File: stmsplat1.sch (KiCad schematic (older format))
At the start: 72 parts, among them CN1 Conn_01x16_Male, CN2 Conn_01x30_Male, CN3 Conn_01x20_Male, CN4 Conn_01x34_Male, J1 Conn_Coaxial, J2 Conn_01x04_Male, J3 Conn_01x04_Male, U1 NUCLEO144-F746ZG, U10 MPL315A2, U11 XBee3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

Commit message: 2nd go at manual routing. Via sizes may all be small.
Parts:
- added C21: 100uF, Capacitor_THT:CP_Radial_D5.0mm_P2.50mm, symbol Device:CP
- U11: symbol splatlib:XBee3 -> stmsplat1-rescue:XBee3-splatlib
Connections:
- net 5V0 is gone; now on net +5V: J2.1 (Pin_1), J3.1 (Pin_1)
- net +5V: now also C21.1
- net GND: now also C21.2
- net at D8.2 (A): now also U11.5 (~RESET)
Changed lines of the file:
@@
 	7550 10450 7900 10450
 Text HLabel 7900 10150 2    50   Input ~ 0
-5V0
++5V
 Text HLabel 7900 10250 2    50   Input ~ 0
 PC12
@@
 	8350 8100 8350 8000
 $Comp
-L splatlib:XBee3 U11
+L stmsplat1-rescue:XBee3-splatlib U11
 U 1 1 5BFA172B
 P 7350 7600
@@
 Connection ~ 12250 8950
 Wire Wire Line
-	10700 8250 10300 8250
+	10700 8250 10500 8250
 $Comp
 L Device:C C20
@@
 	7550 9600 7900 9600
 Text HLabel 7900 9300 2    50   Input ~ 0
-5V0
++5V
 Text HLabel 7900 9400 2    50   Input ~ 0
 PD6
@@
 Wire Wire Line
 	8500 6400 8500 6200
+$Comp
+L Device:CP C21
+U 1 1 5C1EE7CD
+P 10500 8700
+F 0 "C21" H 10618 8746 50  0000 L CNN
+F 1 "100uF" H 10618 8655 50  0000 L CNN
+F 2 "Capacitor_THT:CP_Radial_D5.0mm_P2.50mm" H 10538 8550 50  0001 C CNN
+F 3 "~" H 10500 8700 50  0001 C CNN
+	1    10500 8700
+	1    0    0    -1
+$EndComp
+Wire Wire Line
+	10500 8850 10500 8950
+Wire Wire Line
+	11000 8950 10500 8950
+Connection ~ 11000 8950
+Wire Wire Line
+	10500 8550 10500 8250
+Connection ~ 10500 8250
+Wire Wire Line
+	10500 8250 10300 8250
 $EndSCHEMATC

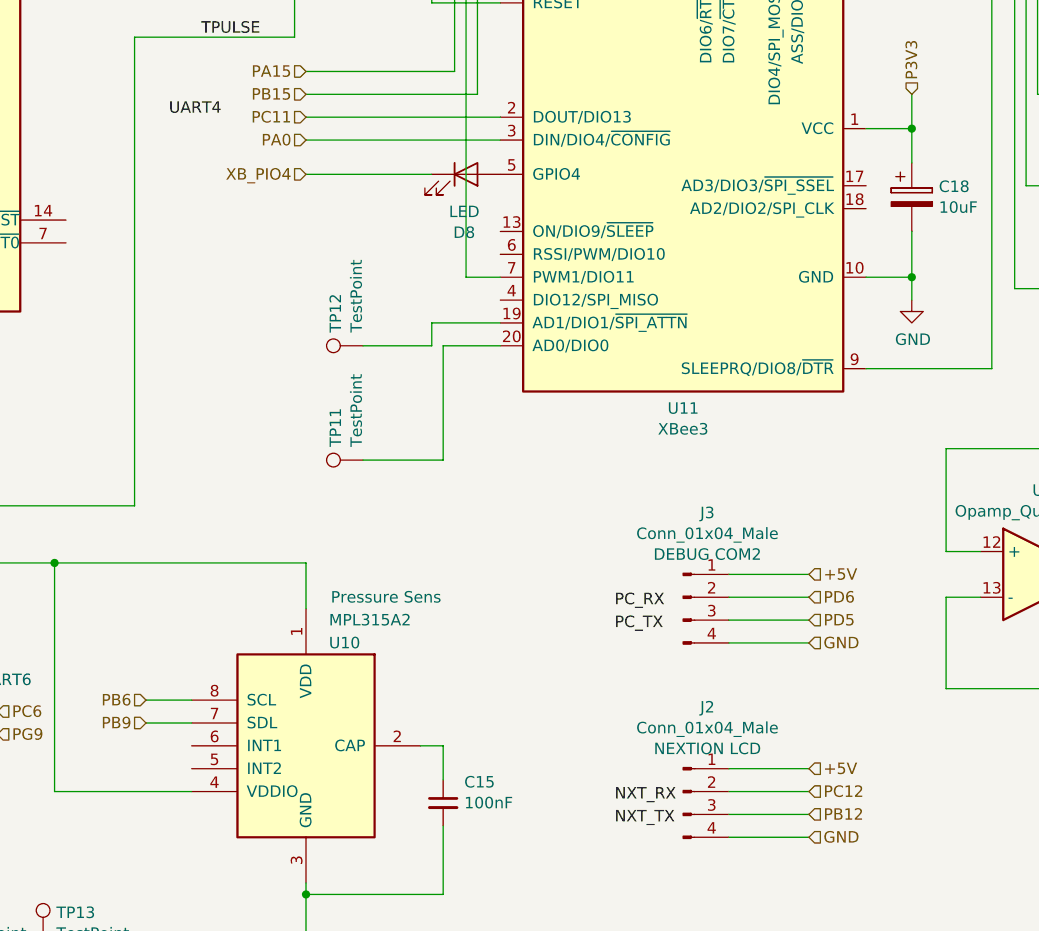
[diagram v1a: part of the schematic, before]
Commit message: Fix Xbee extra symbol pin, change via sizes on power
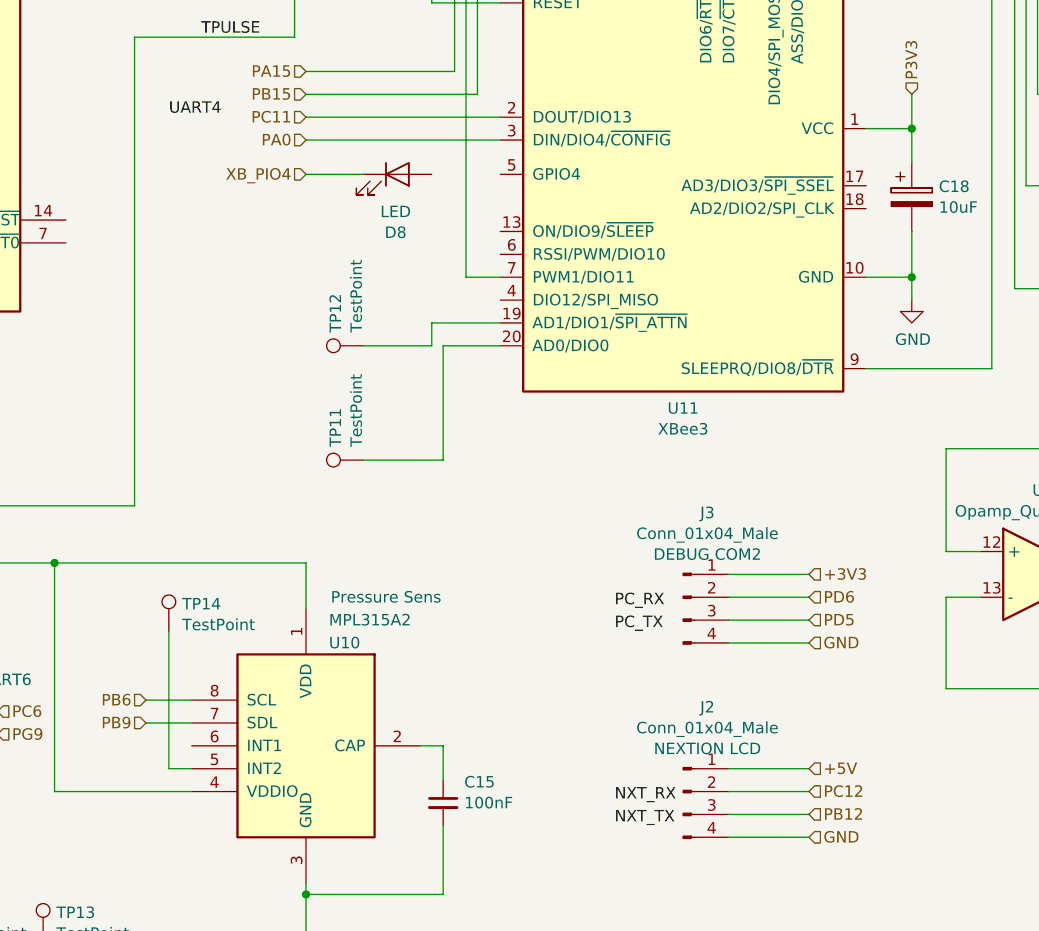
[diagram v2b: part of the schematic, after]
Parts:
- added TP14: TestPoint, TestPoint:TestPoint_Loop_D1.80mm_Drill1.0mm_Beaded, symbol Connector:TestPoint
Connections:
- net +3V3: now also J3.1 (Pin_1)
- net +5V: no longer J3.1 (Pin_1)
- net at U10.5 (INT2): now also TP14.1
- net at D8.2 (A): no longer U11.5 (~RESET)
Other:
- moved on the sheet: D8
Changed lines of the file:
@@
 L Device:LED D8
 U 1 1 5C2D017B
-P 6400 7550
-F 0 "D8" H 6392 7295 50  0000 C CNN
-F 1 "LED" H 6392 7386 50  0000 C CNN
-F 2 "LED_SMD:LED_PLCC-2" H 6400 7550 50  0001 C CNN
-F 3 "~" H 6400 7550 50  0001 C CNN
-	1    6400 7550
-	1    0    0    -1
-$EndComp
-Wire Wire Line
-	6250 7550 5700 7550
+P 6100 7550
+F 0 "D8" H 6092 7295 50  0000 C CNN
+F 1 "LED" H 6092 7386 50  0000 C CNN
+F 2 "LED_SMD:LED_PLCC-2" H 6100 7550 50  0001 C CNN
+F 3 "~" H 6100 7550 50  0001 C CNN
+	1    6100 7550
+	1    0    0    -1
+$EndComp
+Wire Wire Line
+	5950 7550 5700 7550
 Text HLabel 13250 1400 0    50   Input ~ 0
 XB_PIO4
@@
 	7550 9600 7900 9600
 Text HLabel 7900 9300 2    50   Input ~ 0
-+5V
++3V3
 Text HLabel 7900 9400 2    50   Input ~ 0
 PD6
@@
 Wire Wire Line
 	10500 8250 10300 8250
+$Comp
+L Connector:TestPoint TP14
+U 1 1 5C244655
+P 5100 9550
+F 0 "TP14" H 5158 9670 50  0000 L CNN
+F 1 "TestPoint" H 5158 9579 50  0000 L CNN
+F 2 "TestPoint:TestPoint_Loop_D1.80mm_Drill1.0mm_Beaded" H 5300 9550 50  0001 C CNN
+F 3 "~" H 5300 9550 50  0001 C CNN
+	1    5100 9550
+	1    0    0    -1
+$EndComp
+Wire Wire Line
+	5200 10150 5100 10150
+Wire Wire Line
+	5100 10150 5100 9550
 $EndSCHEMATC

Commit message: Update schematic
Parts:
- removed U11: XBee3, spatboard:XBEE-22MM-TH, symbol stmsplat1-rescue:XBee3-splatlib
- added U11: XBee3, spatboard:XBEE-22MM-TH, symbol splatlib:XBee3
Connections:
- net GND: now also U11.10 (GND)
- net P3V3: now also U11.1 (VCC)
- net PA0: now also U11.3 (DIN/DIO4/~CONFIG)
- net PA15: now also U11.12 (DIO7/~CTS)
- net PB15: now also U11.16 (DIO6/~RTS)
- net PC11: now also U11.2 (DOUT/DIO13)
- net PE10: now also U11.9 (SLEEPRQ/DIO8/~DTR)
- net PE15: now also U11.5 (~RESET)
- net at TP12.1: now also U11.19 (AD1/DIO1/~SPI_ATTN)
- net at TP11.1: now also U11.20 (AD0/DIO0)
- net at U8.9: now also U11.7 (PWM1/DIO11)
- net at D8.2 (A): now also U11.13 (ON/DIO9/~SLEEP)
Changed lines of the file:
@@
 Wire Wire Line
 	8350 8100 8350 8000
-$Comp
-L stmsplat1-rescue:XBee3-splatlib U11
-U 1 1 5BFA172B
-P 7350 7600
-F 0 "U11" H 7350 6626 50  0000 C CNN
-F 1 "XBee3" H 7350 6535 50  0000 C CNN
-F 2 "spatboard:XBEE-22MM-TH" H 7500 7700 50  0001 C CNN
-F 3 "http://www.ti.com/lit/gpn/cc2520" H 7350 7350 50  0001 C CNN
-	1    7350 7600
-	1    0    0    -1
-$EndComp
 Wire Wire Line
 	7550 6600 7550 6400
@@
 Wire Wire Line
 	5100 10150 5100 9550
+$Comp
+L splatlib:XBee3 U11
+U 1 1 5C4E2737
+P 7350 7600
+F 0 "U11" H 7350 6626 50  0000 C CNN
+F 1 "XBee3" H 7350 6535 50  0000 C CNN
+F 2 "spatboard:XBEE-22MM-TH" H 7500 7700 50  0001 C CNN
+F 3 "http://www.ti.com/lit/gpn/cc2520" H 7350 7350 50  0001 C CNN
+	1    7350 7600
+	1    0    0    -1
+$EndComp
+Wire Wire Line
+	6550 7800 6350 7800
+Wire Wire Line
+	6350 7800 6350 7550
+Wire Wire Line
+	6350 7550 6250 7550
 $EndSCHEMATC

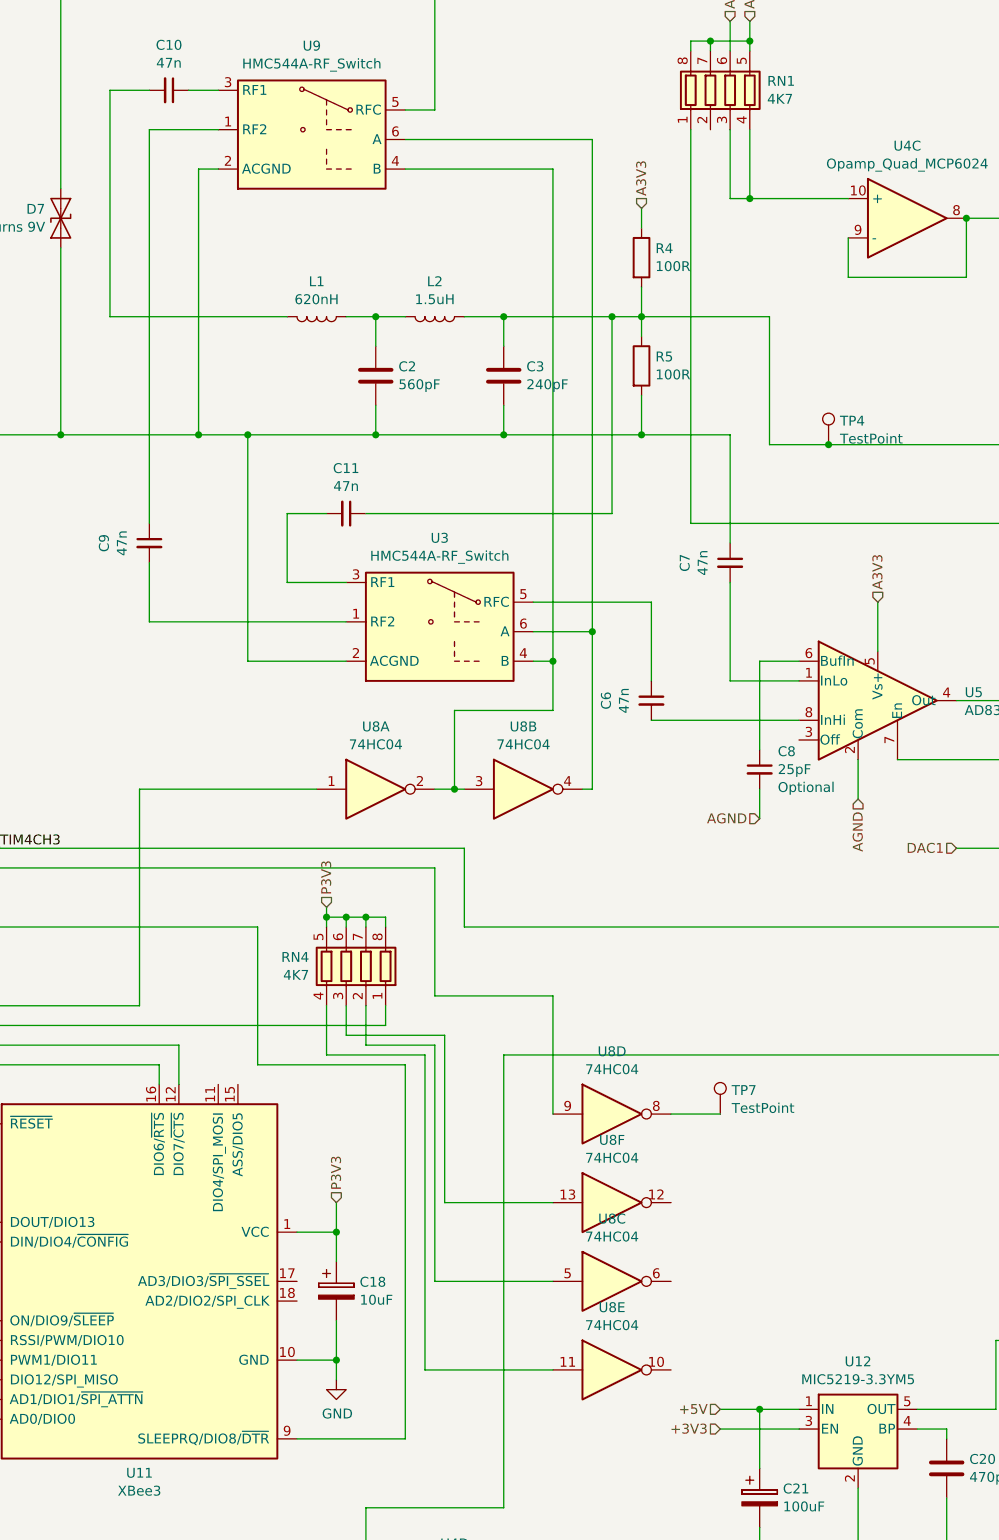
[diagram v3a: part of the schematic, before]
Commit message: Split drive to RF switches
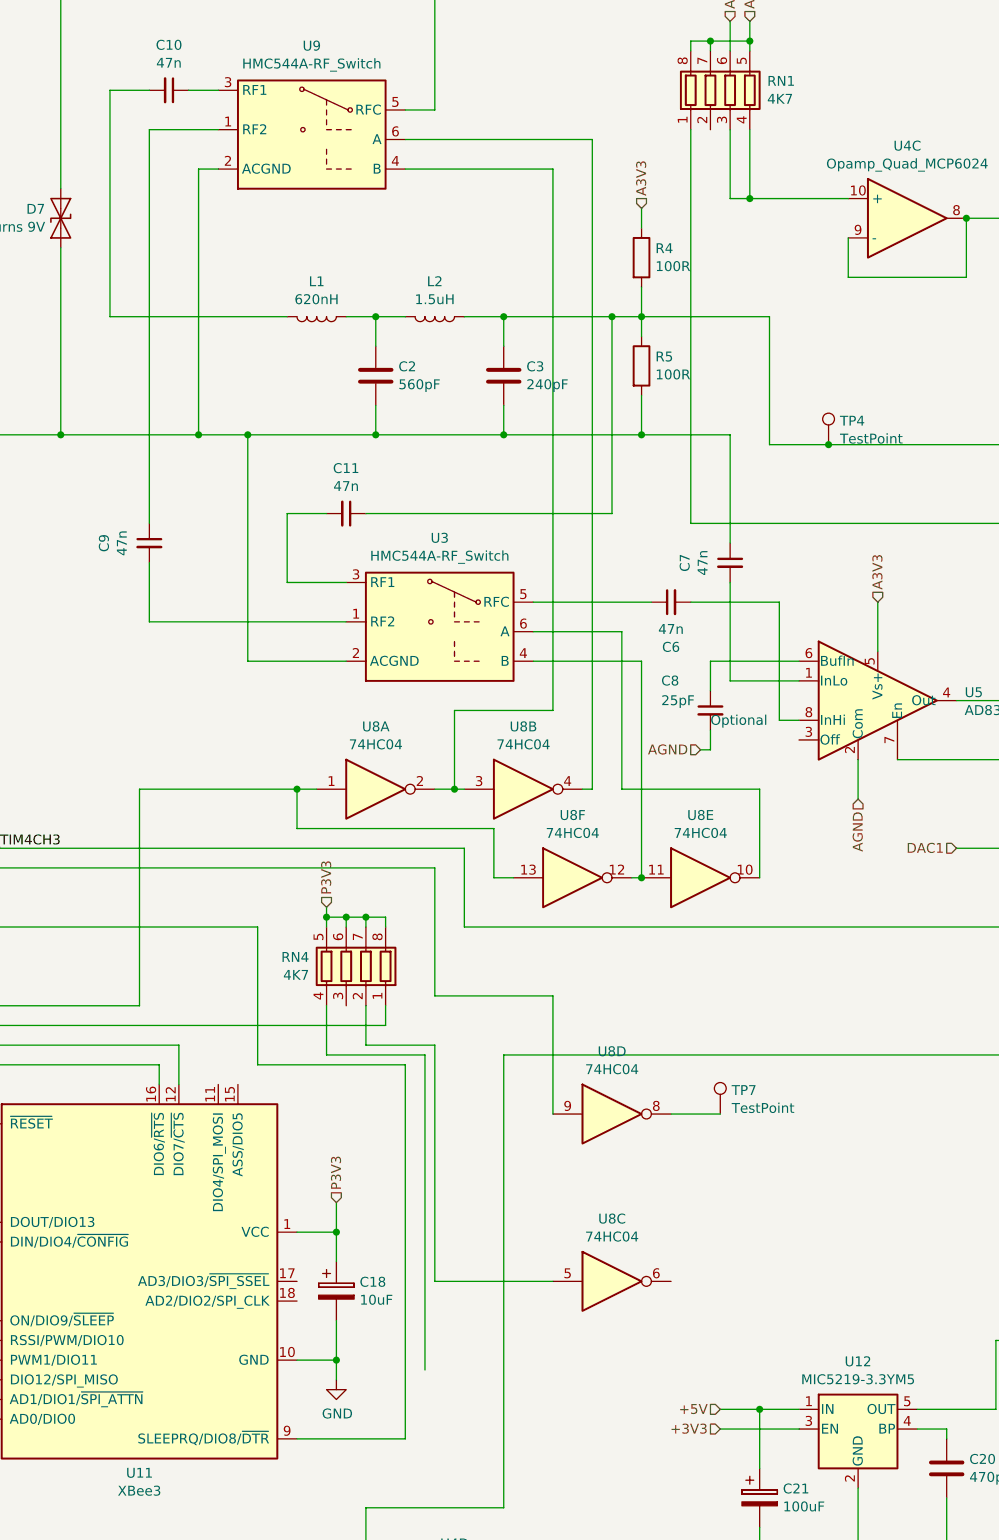
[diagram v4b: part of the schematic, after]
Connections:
- net PE14: now also U8.13
- net at U8.2, U8.3, U9.4 (B): no longer U3.4 (B)
- net at U8.4, U9.6 (A): no longer U3.6 (A)
- net at U8.10: now also U3.6 (A)
- net at U8.11: now also U3.4 (B), U8.12; no longer RN4.4 (R4.1)
- net at RN4.3 (R3.1): no longer U8.13
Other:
- moved on the sheet: C6, C8, U8E, U8F
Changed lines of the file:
@@
 L Device:C_Small C6
 U 1 1 5BFDF984
-P 9950 4650
-F 0 "C6" V 9721 4650 50  0000 C CNN
-F 1 "47n" V 9812 4650 50  0000 C CNN
-F 2 "Capacitor_SMD:C_1210_3225Metric_Pad1.42x2.65mm_HandSolder" H 9950 4650 50  0001 C CNN
-F 3 "~" H 9950 4650 50  0001 C CNN
-	1    9950 4650
-	1    0    0    -1
+P 10050 4150
+F 0 "C6" V 9821 4150 50  0000 C CNN
+F 1 "47n" V 9912 4150 50  0000 C CNN
+F 2 "Capacitor_SMD:C_1210_3225Metric_Pad1.42x2.65mm_HandSolder" H 10050 4150 50  0001 C CNN
+F 3 "~" H 10050 4150 50  0001 C CNN
+	1    10050 4150
+	0    -1   -1   0
 $EndComp
 Wire Wire Line
@@
 	6950 2350 6950 3300
 Connection ~ 6950 3300
-$Comp
-L Device:C_Small C8
-U 1 1 5BEE1C9A
-P 10500 5000
-F 0 "C8" H 10592 5091 50  0000 L CNN
-F 1 "25pF" H 10592 5000 50  0000 L CNN
-F 2 "Capacitor_THT:C_Disc_D7.5mm_W2.5mm_P5.00mm" H 10500 5000 50  0001 C CNN
-F 3 "~" H 10500 5000 50  0001 C CNN
-F 4 "Optional" H 10592 4909 50  0000 L CNN "Option"
-	1    10500 5000
-	1    0    0    -1
-$EndComp
-Wire Wire Line
-	10500 5100 10500 5250
-Text HLabel 10500 5250 0    50   Input ~ 0
+Text HLabel 10200 4900 0    50   Input ~ 0
 AGND
-Wire Wire Line
-	10700 4450 10500 4450
-Wire Wire Line
-	10500 4450 10500 4900
 $Comp
 L 74xx:74HC04 U8
@@
 Connection ~ 11550 2200
 Wire Wire Line
-	9950 4150 9950 4550
-Wire Wire Line
 	7750 1950 7650 1950
 Wire Wire Line
@@
 L 74xx:74HC04 U8
 U 5 1 5C133549
-P 9750 8050
-F 0 "U8" H 9750 8367 50  0000 C CNN
-F 1 "74HC04" H 9750 8276 50  0000 C CNN
-F 2 "" H 9750 8050 50  0001 C CNN
-F 3 "http://www.nxp.com/documents/data_sheet/74HC_HCT04.pdf" H 9750 8050 50  0001 C CNN
-	5    9750 8050
+P 10200 5550
+F 0 "U8" H 10200 5867 50  0000 C CNN
+F 1 "74HC04" H 10200 5776 50  0000 C CNN
+F 2 "" H 10200 5550 50  0001 C CNN
+F 3 "http://www.nxp.com/documents/data_sheet/74HC_HCT04.pdf" H 10200 5550 50  0001 C CNN
+	5    10200 5550
 	1    0    0    -1
 $EndComp
@@
 L 74xx:74HC04 U8
 U 6 1 5C133550
-P 9750 7200
-F 0 "U8" H 9750 7517 50  0000 C CNN
-F 1 "74HC04" H 9750 7426 50  0000 C CNN
-F 2 "" H 9750 7200 50  0001 C CNN
-F 3 "http://www.nxp.com/documents/data_sheet/74HC_HCT04.pdf" H 9750 7200 50  0001 C CNN
-	6    9750 7200
+P 9550 5550
+F 0 "U8" H 9550 5867 50  0000 C CNN
+F 1 "74HC04" H 9550 5776 50  0000 C CNN
+F 2 "" H 9550 5550 50  0001 C CNN
+F 3 "http://www.nxp.com/documents/data_sheet/74HC_HCT04.pdf" H 9550 5550 50  0001 C CNN
+	6    9550 5550
 	1    0    0    -1
 $EndComp
 Wire Wire Line
 	9600 5100 9650 5100
-Wire Wire Line
-	9650 5100 9650 4300
-Wire Wire Line
-	9650 4300 9350 4300
-Wire Wire Line
-	9350 4450 9450 4450
-Wire Wire Line
-	9450 4450 9450 4700
 Wire Wire Line
 	9450 4700 8950 4700
@@
 	8200 950  8850 950
 Wire Wire Line
-	9650 4300 9650 1800
-Wire Wire Line
 	9650 1800 8700 1800
-Connection ~ 9650 4300
-Wire Wire Line
-	9450 4450 9450 1950
 Wire Wire Line
 	8700 1950 9450 1950
-Connection ~ 9450 4450
 Connection ~ 10850 3350
 Wire Wire Line
@@
 NXT_RX
 Wire Wire Line
-	8250 5100 7350 5100
+	8250 5100 8150 5100
 Wire Wire Line
 	7350 5100 7350 6200
@@
 	13550 8950 13900 8950
 Wire Wire Line
-	9450 8050 8800 8050
-Wire Wire Line
 	8800 8050 8800 6450
 Wire Wire Line
@@
 Wire Wire Line
 	8850 6400 8500 6400
-Wire Wire Line
-	9450 7200 8900 7200
-Wire Wire Line
-	8900 7200 8900 6350
 Wire Wire Line
 	8400 5750 8500 5750
@@
 Wire Wire Line
 	10350 4050 10350 4550
-Wire Wire Line
-	9950 4750 10700 4750
 Wire Wire Line
 	6150 950  6400 950
@@
 	5650 6300 8600 6300
 Wire Wire Line
-	8400 6350 8400 6200
-Wire Wire Line
-	8400 6350 8900 6350
-Wire Wire Line
 	8500 6400 8500 6200
 $Comp
@@
 Wire Wire Line
 	6350 7550 6250 7550
+Wire Wire Line
+	9450 1950 9450 4700
+Wire Wire Line
+	9350 4450 9900 4450
+Wire Wire Line
+	9900 4450 9900 5550
+Wire Wire Line
+	9900 5550 9850 5550
+Wire Wire Line
+	8150 5100 8150 5300
+Wire Wire Line
+	8150 5300 9150 5300
+Wire Wire Line
+	9150 5300 9150 5550
+Wire Wire Line
+	9150 5550 9250 5550
+Connection ~ 8150 5100
+Wire Wire Line
+	8150 5100 7350 5100
+Wire Wire Line
+	9650 1800 9650 5100
+Connection ~ 9900 5550
+$Comp
+L Device:C_Small C8
+U 1 1 5BEE1C9A
+P 10250 4700
+F 0 "C8" H 10000 4850 50  0000 L CNN
+F 1 "25pF" H 10000 4750 50  0000 L CNN
+F 2 "Capacitor_THT:C_Disc_D7.5mm_W2.5mm_P5.00mm" H 10250 4700 50  0001 C CNN
+F 3 "~" H 10250 4700 50  0001 C CNN
+F 4 "Optional" H 10250 4650 50  0000 L CNN "Option"
+	1    10250 4700
+	1    0    0    -1
+$EndComp
+Wire Wire Line
+	10700 4450 10250 4450
+Wire Wire Line
+	10250 4900 10200 4900
+Wire Wire Line
+	10150 4150 10600 4150
+Wire Wire Line
+	10600 4150 10600 4750
+Wire Wire Line
+	10600 4750 10700 4750
+Wire Wire Line
+	9800 5100 9800 4300
+Wire Wire Line
+	9800 4300 9350 4300
+Wire Wire Line
+	10500 5550 10500 5100
+Wire Wire Line
+	9800 5100 10500 5100
+Wire Wire Line
+	10250 4450 10250 4600
+Wire Wire Line
+	10250 4800 10250 4900
 $EndSCHEMATC

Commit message: Prepared for PCB production
Several PCB tracking changes and footprint tweaks etc
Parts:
- J2, J3: footprint Connector_PinHeader_2.54mm:PinHeader_1x04_P2.54mm_Vertical -> spatboard:PinHeader_1x04_P2.54mm_Vertical
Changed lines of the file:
@@
 F 0 "J2" H 7456 10619 50  0000 C CNN
 F 1 "Conn_01x04_Male" H 7456 10528 50  0000 C CNN
-F 2 "Connector_PinHeader_2.54mm:PinHeader_1x04_P2.54mm_Vertical" H 7350 10250 50  0001 C CNN
+F 2 "spatboard:PinHeader_1x04_P2.54mm_Vertical" H 7350 10250 50  0001 C CNN
 F 3 "~" H 7350 10250 50  0001 C CNN
 F 4 "NEXTION LCD" H 7456 10437 50  0000 C CNN "DESC"
@@
 F 0 "J3" H 7456 9769 50  0000 C CNN
 F 1 "Conn_01x04_Male" H 7456 9678 50  0000 C CNN
-F 2 "Connector_PinHeader_2.54mm:PinHeader_1x04_P2.54mm_Vertical" H 7350 9400 50  0001 C CNN
+F 2 "spatboard:PinHeader_1x04_P2.54mm_Vertical" H 7350 9400 50  0001 C CNN
 F 3 "~" H 7350 9400 50  0001 C CNN
 F 4 "DEBUG COM2" H 7456 9587 50  0000 C CNN "DESC"
